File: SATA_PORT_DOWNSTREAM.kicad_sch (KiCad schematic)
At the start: 13 parts, among them CN1 HDGCYLSY-SATA-113, Q1 2N7002, Q2 2N7002, Q3 2N7002

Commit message: Cleaned up schematic and replaced TC358743XBG with reverse-engineered LT6911C
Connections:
- net +3V3: no longer C28.2, R4.2
- new net: C28.2, R4.2

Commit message: Added TVS clamping diodes to upstream USB-C port and fixed RX/TX orientation routing for entire system
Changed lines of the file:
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@@
 	)
 	(hierarchical_label "RX-"
-		(shape output)
+		(shape input)
 		(at 73.66 48.26 180)
 		(effects
@@
 	)
 	(hierarchical_label "RX+"
-		(shape output)
+		(shape input)
 		(at 88.9 49.53 0)
 		(effects
@@
 	)
 	(hierarchical_label "TX-"
-		(shape input)
+		(shape output)
 		(at 73.66 45.72 180)
 		(effects
@@
 	)
 	(hierarchical_label "TX+"
-		(shape input)
+		(shape output)
 		(at 88.9 44.45 0)
 		(effects

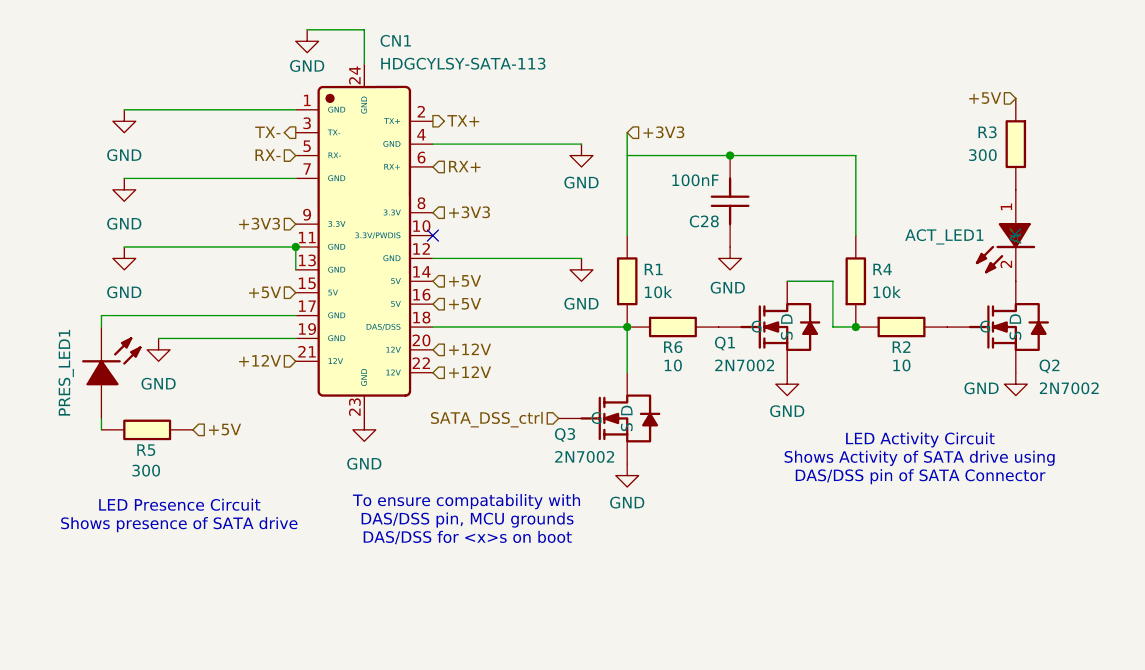
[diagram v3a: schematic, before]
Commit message: Basic Function Review/Documentation for LT6911C Subsystem
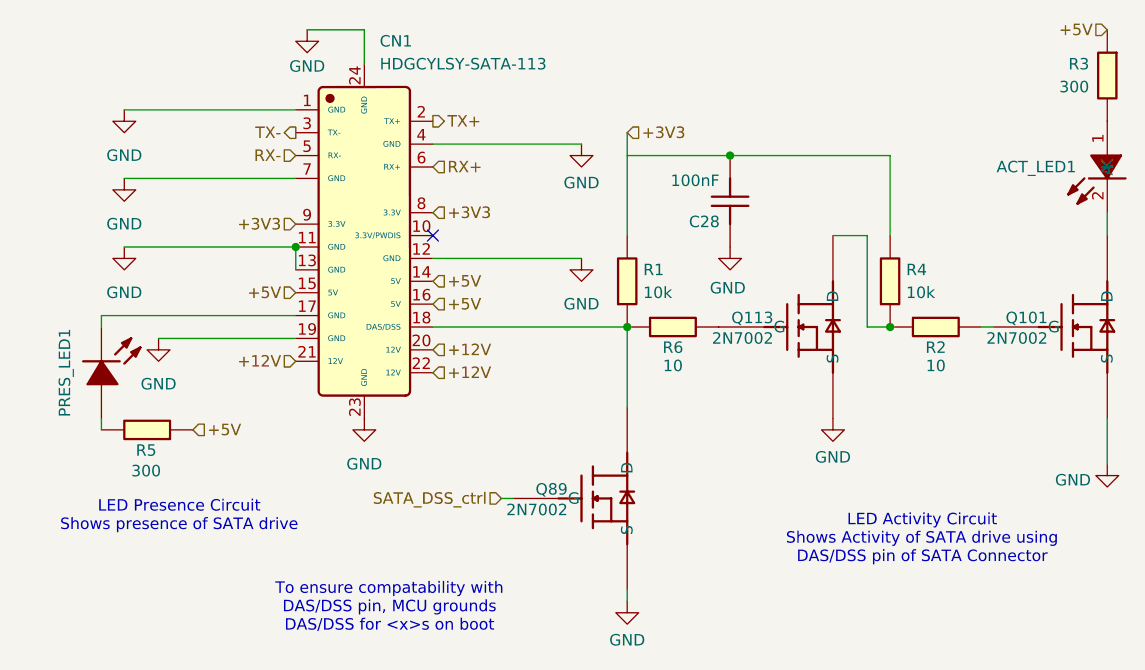
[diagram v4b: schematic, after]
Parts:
- removed Q1, Q2, Q3: 2N7002, Package_TO_SOT_SMD:SOT-23-3, symbol JLCImport:2N7002
- added Q101, Q113, Q89: 2N7002, JLCImport:2N7002_C916396, symbol JLCImport:2N7002_C916396
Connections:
- net GND: now also Q101.2 (S), Q113.2 (S), Q89.2 (S)
- net SATA_DSS_ctrl: now also Q89.1 (G)
- net at CN1.18 (DAS/DSS), R1.1, R6.1: now also Q89.3 (D)
- net at R6.2: now also Q113.1 (G)
- net at R2.1, R4.1: now also Q113.3 (D)
- net at R2.2: now also Q101.1 (G)
- net at ACT_LED1.2 (K): now also Q101.3 (D)
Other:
- moved on the sheet: ACT_LED1, R2, R3, R4

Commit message: Basic Function Review/Documentation of RP2354B
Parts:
- removed PRES_LED1: whiteLEDSMD, JLCImport:whiteLEDSMD, symbol JLCImport:whiteLEDSMD
- removed R5: 300, Resistor_SMD:R_0603_1608Metric, symbol JLCImport:0603WAF3000T5E
- added LED1: White, JLCImport:GL0603UW01, symbol JLCImport:GL0603UW01
- added R5: 1k, Resistor_SMD:R_0402_1005Metric, symbol JLCImport:0402WGF1001TCE
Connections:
- net +5V: now also R5.2
- net at CN1.17 (GND): now also LED1.2 (C)
- new net: LED1.1 (A), R5.1
